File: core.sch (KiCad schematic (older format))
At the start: 1 part, among them J1 DIMM204

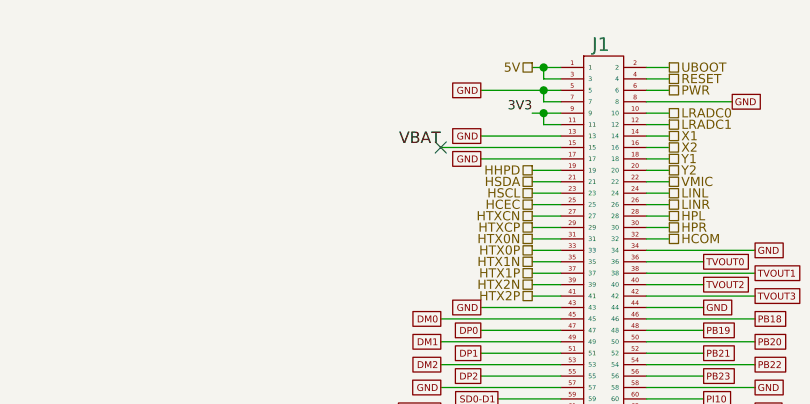
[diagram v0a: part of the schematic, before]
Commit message: 1.4
Fix some issues
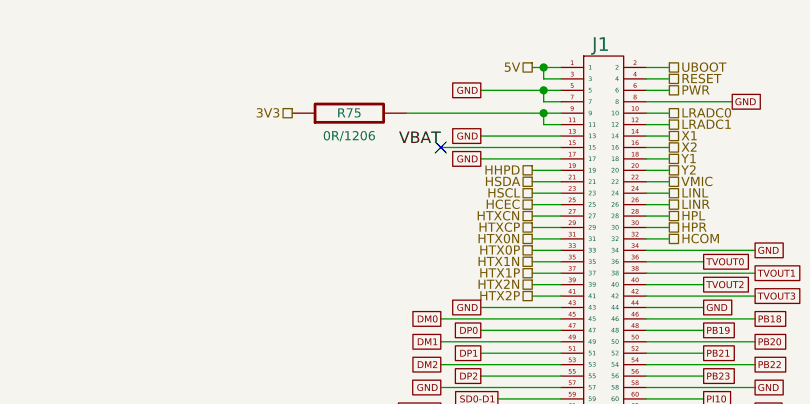
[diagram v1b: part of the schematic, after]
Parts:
- added R75: 0R/1206, ~, symbol R
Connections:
- net 3V3: now also R75.1; no longer J1.11, J1.9
- new net: J1.11, J1.9, R75.2
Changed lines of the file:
@@
 Sheet 2 11
 Title ""
-Date "19 sep 2014"
+Date "25 nov 2014"
 Rev ""
 Comp ""
@@
 Connection ~ 5900 1650
 Wire Wire Line
-	5850 1750 5975 1750
+	5300 1750 5975 1750
 Wire Wire Line
 	5975 1800 5900 1800
@@
 VBAT
 NoConn ~ 5450 1900
-Text Label 5850 1750 2    40   ~ 0
+$Comp
+L R R75
+U 1 1 544DDFFF
+P 5050 1750
+F 0 "R75" V 5050 1750 40  0000 C CNN
+F 1 "0R/1206" V 4950 1750 40  0000 C CNN
+F 2 "~" V 4980 1750 30  0000 C CNN
+F 3 "~" H 5050 1750 30  0000 C CNN
+	1    5050 1750
+	0    -1   -1   0
+$EndComp
+Text HLabel 4800 1750 0    40   UnSpc ~ 0
 3V3
 $EndSCHEMATC
